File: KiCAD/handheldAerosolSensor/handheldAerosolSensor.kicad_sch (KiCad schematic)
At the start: 13 parts, among them J1 PWR IN, J2 PUSH BUTTON, J3 MCU, J4 MCU, Q1 IRF4905, Q2 2N7000

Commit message: Initial Commit
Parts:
- added J5: DC/DC Bootser, symbol Connector:Conn_01x02_Pin
- added J6: PWR OUT 5volt, symbol Connector:Conn_01x02_Socket
- J1: value PWR IN -> BAT IN (3.7v)
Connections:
- net GND: now also J5.2 (Pin_2), J6.1 (Pin_1)
- net at J3.1 (Pin_1), Q1.2 (D): now also J5.1 (Pin_1), J6.2 (Pin_2)
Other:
- note added: "DC/DC Booster"
- moved on the sheet: A1, C1, D1, D2, J1, J2, J3, J4, Q1, Q2, R1, R2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

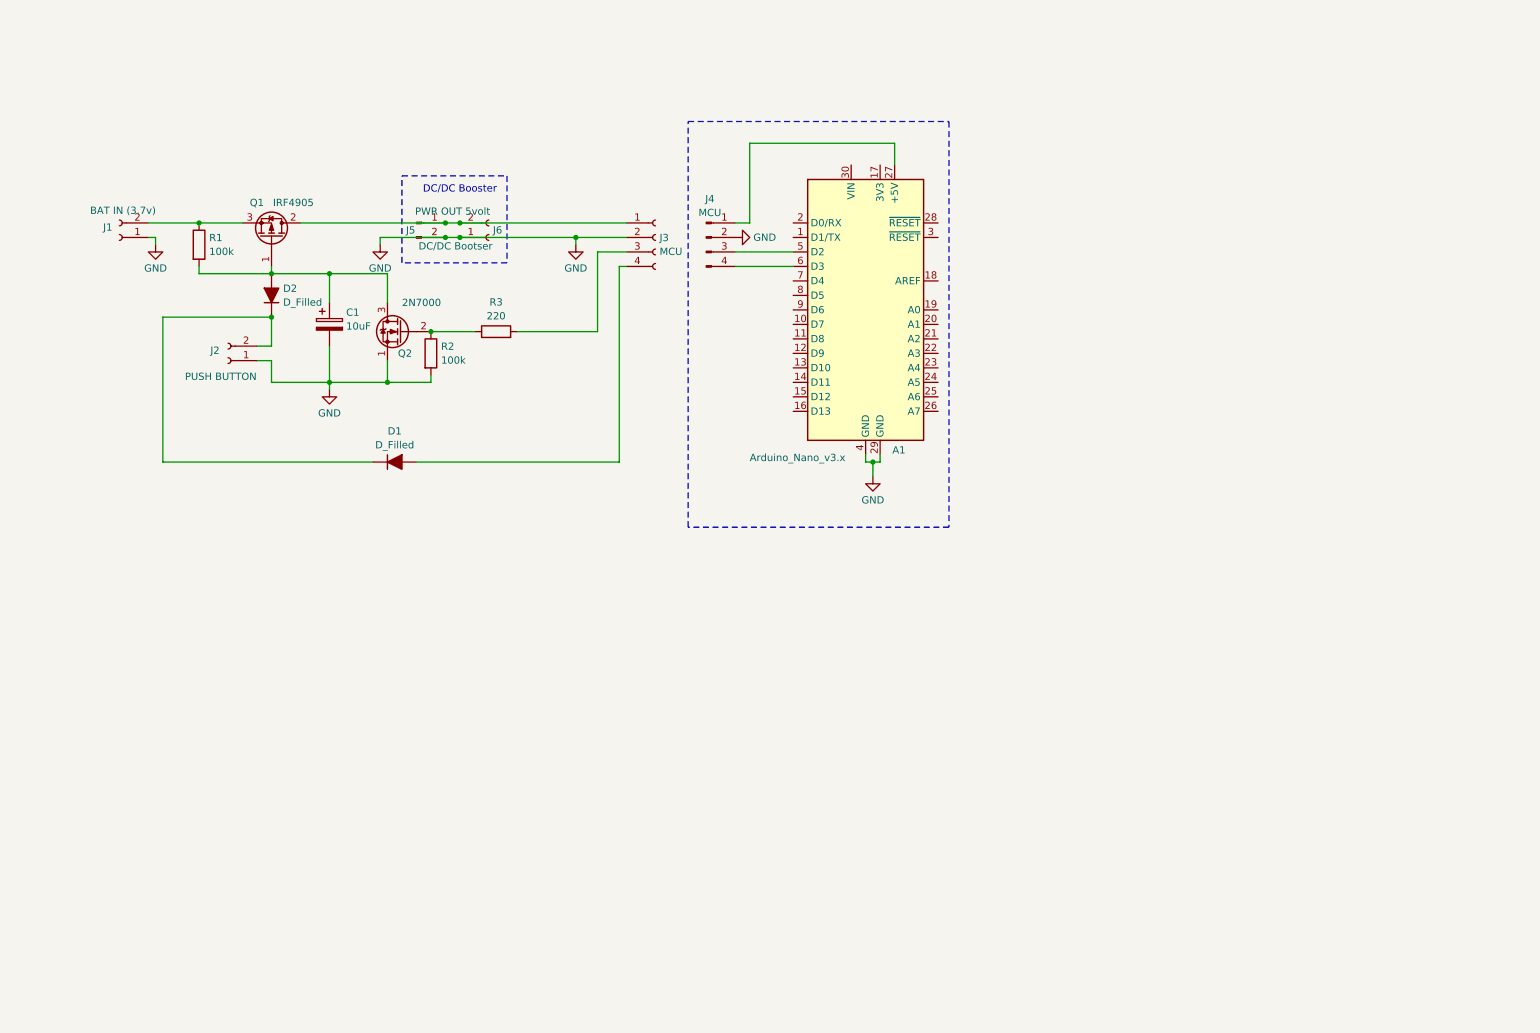
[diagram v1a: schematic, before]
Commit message: Added KiCAD
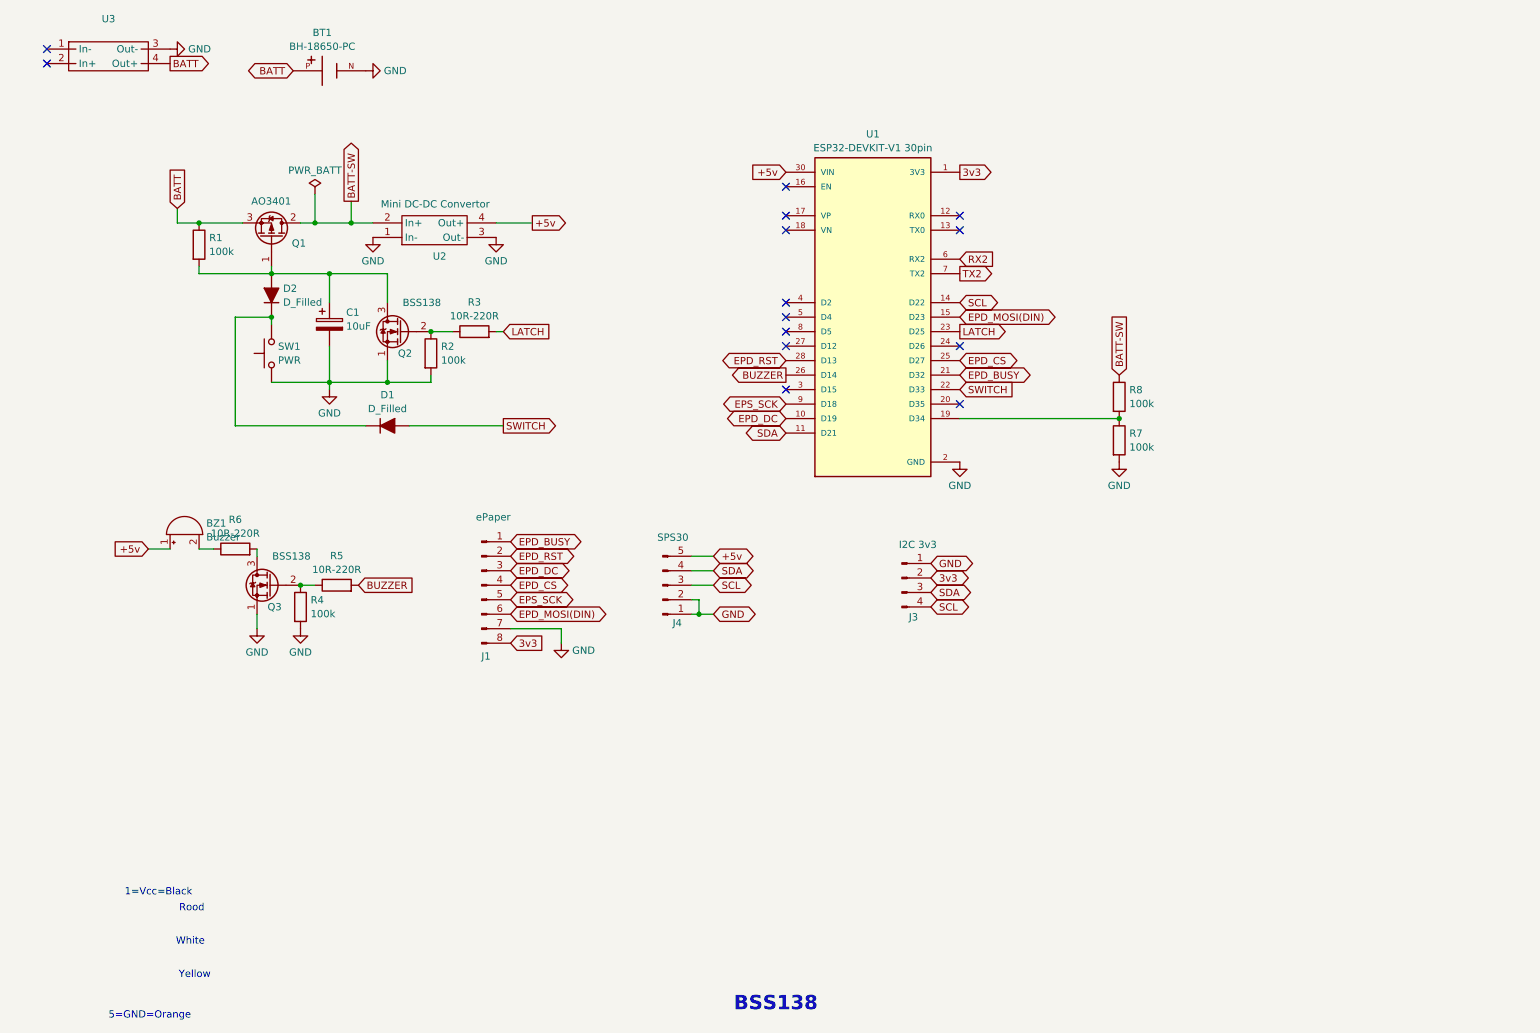
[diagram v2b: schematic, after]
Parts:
- removed A1: Arduino_Nano_v3.x, Module:Arduino_Nano, symbol MCU_Module:Arduino_Nano_v3.x
- removed J1: BAT IN (3.7v), symbol Connector:Conn_01x02_Socket
- removed J2: PUSH BUTTON, symbol Connector:Conn_01x02_Socket
- removed J3: MCU, symbol Connector:Conn_01x04_Socket
- removed J4: MCU, symbol Connector:Conn_01x04_Pin
- removed J5: DC/DC Bootser, symbol Connector:Conn_01x02_Pin
- removed J6: PWR OUT 5volt, symbol Connector:Conn_01x02_Socket
- added BT1: BH-18650-PC, BH-18650-PC:BAT_BH-18650-PC, symbol MyNewLibrary:BH-18650-PC
- added BZ1: Buzzer, Connector_JST:JST_XH_B8B-XH-A_1x08_P2.50mm_Vertical, symbol Device:Buzzer
- added J1: ePaper, Connector_JST:JST_XH_B8B-XH-A_1x08_P2.50mm_Vertical, symbol Connector:Conn_01x08_Pin
- added J3: I2C 3v3, Connector_JST:JST_XH_B4B-XH-A_1x04_P2.50mm_Vertical, symbol Connector:Conn_01x04_Pin
- added J4: SPS30, Connector_JST:JST_XH_B5B-XH-A_1x05_P2.50mm_Vertical, symbol Connector:Conn_01x05_Pin
- added Q3: BSS138, Package_TO_SOT_SMD:SOT-23, symbol Transistor_FET:2N7000
- added R4, R7, R8: 100k, Resistor_SMD:R_1206_3216Metric_Pad1.30x1.75mm_HandSolder, symbol Device:R
- added R5, R6: 10R-220R, Resistor_SMD:R_1206_3216Metric_Pad1.30x1.75mm_HandSolder, symbol Device:R
- added SW1: PWR, Button_Switch_THT:SW_PUSH_6mm_H4.3mm, symbol Switch:SW_Push
- added U1: ESP32-DEVKIT-V1 30pin, MyNewLibrary:MODULE_ESP32_DEVKIT_V1_30pin, symbol MyNewLibrary:ESP32-DEVKIT-V1-30pin
- added U2: Mini DC-DC Convertor, MyNewLibrary:Mini DC-DC Boost Convertor, symbol MyNewLibrary:Mini_DC-DC_Boost_Convertor
- added U3: ~, MyNewLibrary:TP4056_USB-Charger_Board, symbol MyNewLibrary:TP4056Module
- C1: footprint (none) -> Capacitor_SMD:C_1206_3216Metric_Pad1.33x1.80mm_HandSolder
- D1, D2: footprint (none) -> Diode_SMD:D_1206_3216Metric_Pad1.42x1.75mm_HandSolder
- Q1: value IRF4905 -> AO3401; footprint Package_TO_SOT_THT:TO-220-3_Vertical -> Package_TO_SOT_SMD:SOT-23
- Q2: value 2N7000 -> BSS138; footprint Package_TO_SOT_THT:TO-92_Inline -> Package_TO_SOT_SMD:SOT-23
- R1, R2: footprint (none) -> Resistor_SMD:R_1206_3216Metric_Pad1.30x1.75mm_HandSolder
- R3: value 220 -> 10R-220R; footprint (none) -> Resistor_SMD:R_1206_3216Metric_Pad1.30x1.75mm_HandSolder
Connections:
- net GND: now also BT1.N, J1.7 (Pin_7), J3.1 (Pin_1), J4.1 (Pin_1), J4.2 (Pin_2), Q3.1 (S), R4.2, R7.2, SW1.1, U1.2 (GND), U1.29 (GND), U2.1 (In-), U2.3 (Out-), U3.3 (Out-)
- net BATT-SW: now reaches Q1.2 (D)
- net BATT-SW: now also R8.1, U2.2 (In+)
- net BATT: now reaches Q1.3 (S), R1.1
- net BATT: now also BT1.P, U3.4 (Out+)
- net at D1.1 (K), D2.1 (K): now also SW1.2
- net LATCH: now reaches R3.2
- net LATCH: now also U1.23 (D25)
- net SWITCH: now reaches D1.2 (A)
- net SWITCH: now also U1.22 (D33)
- new net: BZ1.2 (-), R6.1
- new net: Q3.3 (D), R6.2
- new net: Q3.2 (G), R4.1, R5.1
- new net: R7.1, R8.2, U1.19 (D34)
- new net +5v: BZ1.1 (+), J4.5 (Pin_5), U1.30 (VIN), U2.4 (Out+)
- new net 3v3: J1.8 (Pin_8), J3.2 (Pin_2), U1.1 (3V3)
- new net BUZZER: R5.2, U1.26 (D14)
- new net EPD_BUSY: J1.1 (Pin_1), U1.21 (D32)
- new net EPD_CS: J1.4 (Pin_4), U1.25 (D27)
- new net EPD_DC: J1.3 (Pin_3), U1.10 (D19)
- new net EPD_MOSI(DIN): J1.6 (Pin_6), U1.15 (D23)
- new net EPD_RST: J1.2 (Pin_2), U1.28 (D13)
- new net EPS_SCK: J1.5 (Pin_5), U1.9 (D18)
- new net RX2: U1.6 (RX2)
- new net SCL: J3.4 (Pin_4), J4.3 (Pin_3), U1.14 (D22)
- new net SDA: J3.3 (Pin_3), J4.4 (Pin_4), U1.11 (D21)
- new net TX2: U1.7 (TX2)
- no-connect marks 0 -> 14
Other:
- note added: "1=Vcc=Black"
- note added: "5=GND=Orange"
- note added: "BSS138"
- note added: "Rood"
- note added: "White"
- note added: "Yellow"
- note removed: "DC/DC Booster"
- company: (none) -> By Willem Aandewiel
- title: (none) -> handheldAerosolSensor
- moved on the sheet: D1, R3

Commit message: feat(hardware): Add buzzer and reorganize PCB net naming
- Add CPI-148-24-90T-67 buzzer/transducer component (LS1)
- Refactor battery net names for consistency (BAT → BATT, BATT-SW)
- Reorganize net numbering and clean up net naming scheme
- Update component references and power connections
- Add new footprint library entry for buzzer transducer
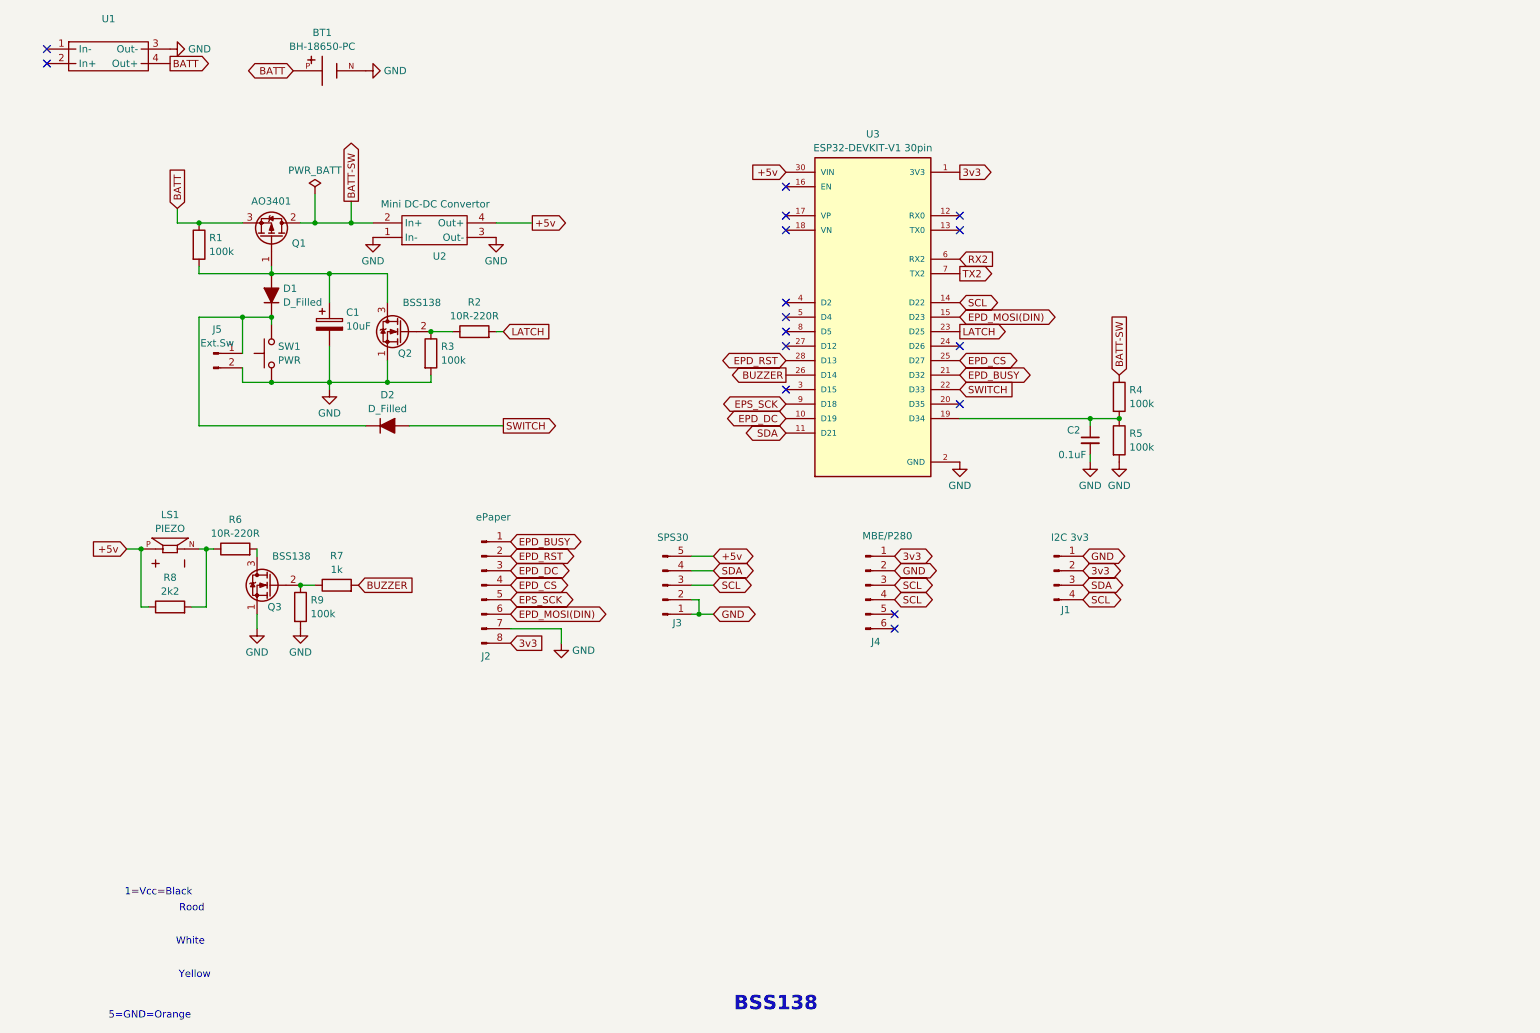
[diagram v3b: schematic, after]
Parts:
- removed BZ1: Buzzer, Connector_JST:JST_XH_B8B-XH-A_1x08_P2.50mm_Vertical, symbol Device:Buzzer
- added C2: 0.1uF, Capacitor_SMD:C_1206_3216Metric_Pad1.33x1.80mm_HandSolder, symbol Device:C_Small
- added J4: MBE/P280, Connector_PinSocket_2.54mm:PinSocket_1x06_P2.54mm_Vertical, symbol Connector:Conn_01x06_Pin
- added J5: Ext.Sw, Connector_JST:JST_XH_B2B-XH-A_1x02_P2.50mm_Vertical, symbol Connector:Conn_01x02_Pin
- added LS1: PIEZO, MyNewLibrary:XDCR_CPI-148-24-90T-67, symbol MyNewLibrary:CPI-148-24-90T-67
- added R8: 2k2, Resistor_SMD:R_1206_3216Metric_Pad1.30x1.75mm_HandSolder, symbol Device:R
- R7: renamed from R5; value 10R-220R -> 1k
- renumbered D2 to D1, D1 to D2, J3 to J1, J1 to J2, J4 to J3, R3 to R2, R2 to R3, R8 to R4, R7 to R5, R4 to R9, U3 to U1, U1 to U3
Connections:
- net +5v: now also LS1.P, R8.1
- net 3v3: now also J4.1 (Pin_1)
- net GND: now also C2.2, J4.2 (Pin_2), J5.2 (Pin_2)
- net SCL: now also J4.3 (Pin_3), J4.4 (Pin_4)
- net at R6.1: now also LS1.N, R8.2
- net at D1.1 (K), D2.1 (K), SW1.2: now also J5.1 (Pin_1)
- net at R4.2, R5.1, U3.19 (D34): now also C2.1
- no-connect marks 14 -> 16
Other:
- moved on the sheet: J1

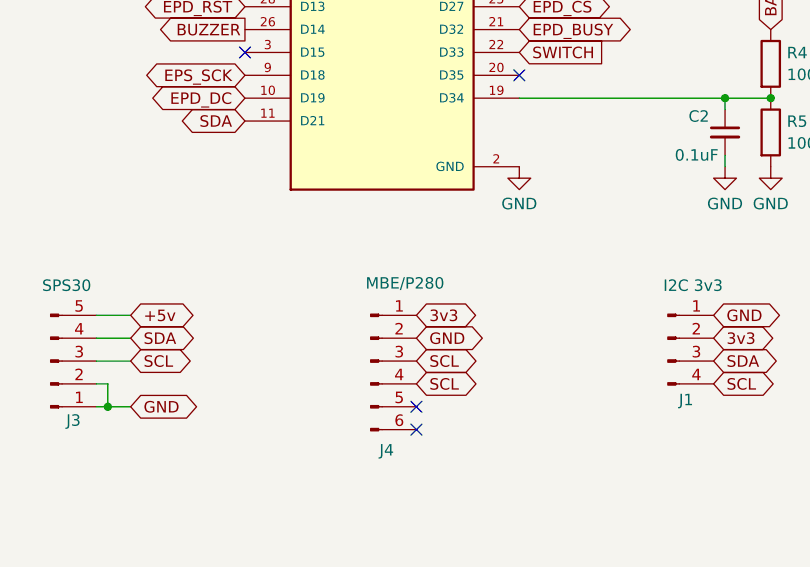
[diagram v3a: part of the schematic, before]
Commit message: feat(kicad): add image to handheld aerosol sensor schematic
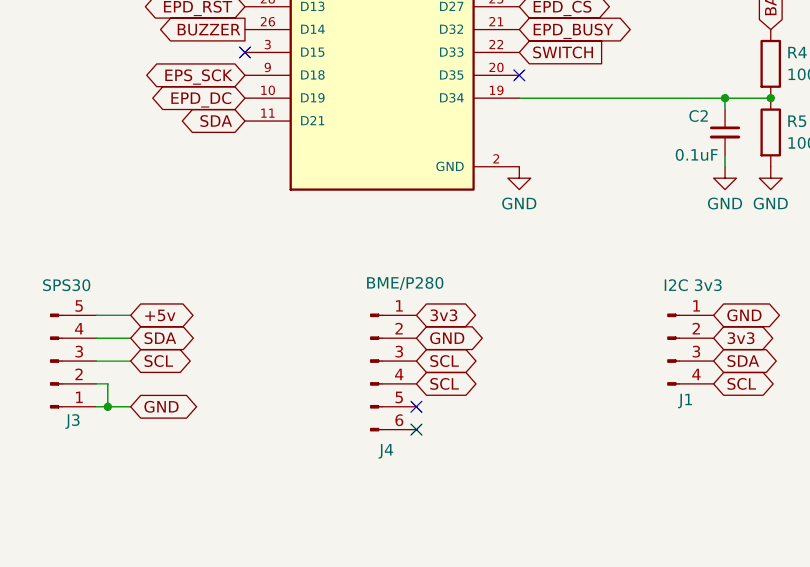
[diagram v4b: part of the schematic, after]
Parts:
- J4: value MBE/P280 -> BME/P280

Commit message: KiCad aanpassingen
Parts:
- removed U1: ~, MyNewLibrary:TP4056_USB-Charger_Board, symbol MyNewLibrary:TP4056Module
- added H1, H2, H3, H4, H5: MountingHole, MountingHole:MountingHole_2.7mm, symbol Mechanical:MountingHole
- added J6: PMS5003, Connector_JST:JST_XH_B8B-XH-A_1x08_P2.50mm_Vertical, symbol Connector:Conn_01x08_Pin
- added R10, R11: 10k, Resistor_SMD:R_1206_3216Metric_Pad1.30x1.75mm_HandSolder, symbol Device:R
- added U1: ~, MyNewLibrary:TP4056_USB-Charger_Board, symbol MyNewLibrary:TP4056module
- D1, D2: value D_Filled -> 1N4148
- R8: value 2k2 -> 100k
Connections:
- net +5v: now also J6.8 (Pin_8)
- net 3v3: now also J1.3 (Pin_3), J2.1 (Pin_1), R10.2, R11.2; no longer J1.2 (Pin_2), J2.8 (Pin_8)
- net EPD_BUSY: now also J2.8 (Pin_8); no longer J2.1 (Pin_1)
- net EPD_CS: now also J2.5 (Pin_5); no longer J2.4 (Pin_4)
- net EPD_DC: now also J2.6 (Pin_6); no longer J2.3 (Pin_3)
- net EPD_MOSI(DIN): now also J2.3 (Pin_3); no longer J2.6 (Pin_6)
- net EPD_RST: now also J2.7 (Pin_7); no longer J2.2 (Pin_2)
- net EPS_SCK: now also J2.4 (Pin_4); no longer J2.5 (Pin_5)
- net GND: now also J1.4 (Pin_4), J2.2 (Pin_2), J6.7 (Pin_7), U1.1 (Out-); no longer BT1.N, J1.1 (Pin_1), J2.7 (Pin_7)
- net SCL: now also J1.1 (Pin_1); no longer J1.4 (Pin_4), J4.4 (Pin_4)
- net SDA: now also J1.2 (Pin_2), J4.4 (Pin_4); no longer J1.3 (Pin_3)
- net PMS5003-RESET: now reaches U3.4 (D2)
- net PMS5003-RESET: now also J6.3 (Pin_3), R11.1
- net PMS5003-SET: now reaches U3.5 (D4)
- net PMS5003-SET: now also J6.6 (Pin_6), R10.1
- net BATT renamed OUT+
- net OUT+: now also U1.4 (Out+); no longer BT1.P
- net RX2 renamed RX2-PMS5003-TX
- net RX2-PMS5003-TX: now also J6.4 (Pin_4)
- net TX2 renamed TX2-PMS5003-RX
- net TX2-PMS5003-RX: now also J6.5 (Pin_5)
- new net B+: BT1.P, U1.3 (Bat+)
- new net B-: BT1.N, U1.2 (Batt-)
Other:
- added sheet PowerLatch (untitled.kicad_sch)
- moved on the sheet: BT1, J1, J3, J4

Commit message: KiCAD design openScad design
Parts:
- removed Q1: AO3401, Package_TO_SOT_SMD:SOT-23, symbol Transistor_FET:IRF4905
- removed Q2, Q3: BSS138, Package_TO_SOT_SMD:SOT-23, symbol Transistor_FET:2N7000
- added Q101: AO3401A, MyNewLibrary:AO3401, symbol MyNewLibrary:AO3401A
- added Q102, Q103: BSS138, MyNewLibrary:BSS138, symbol MyNewLibrary:BSS138
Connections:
- net BATT-SW: now also Q101.3
- net GND: now also Q102.2, Q103.2
- net OUT+: now also Q101.2
- net at R2.1, R3.1: now also Q103.1
- net at C1.1, D1.2 (A), R1.2: now also Q101.1, Q103.3
- net at R6.2: now also Q102.3
- net at R7.1, R9.1: now also Q102.1
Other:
- removed sheet PowerLatch
- moved on the sheet: R7, R9
